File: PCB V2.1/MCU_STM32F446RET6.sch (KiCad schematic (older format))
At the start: 37 parts, among them J1 20021121-00010C4LF, J2 0475890001-MicroUSBPort, SW1 B3U-1000P, U1 STM32F446RET6_-_TQFP64, X1 ABM3B8.000MHZB2T, X2 ABS07-32.768KHZ-9-T

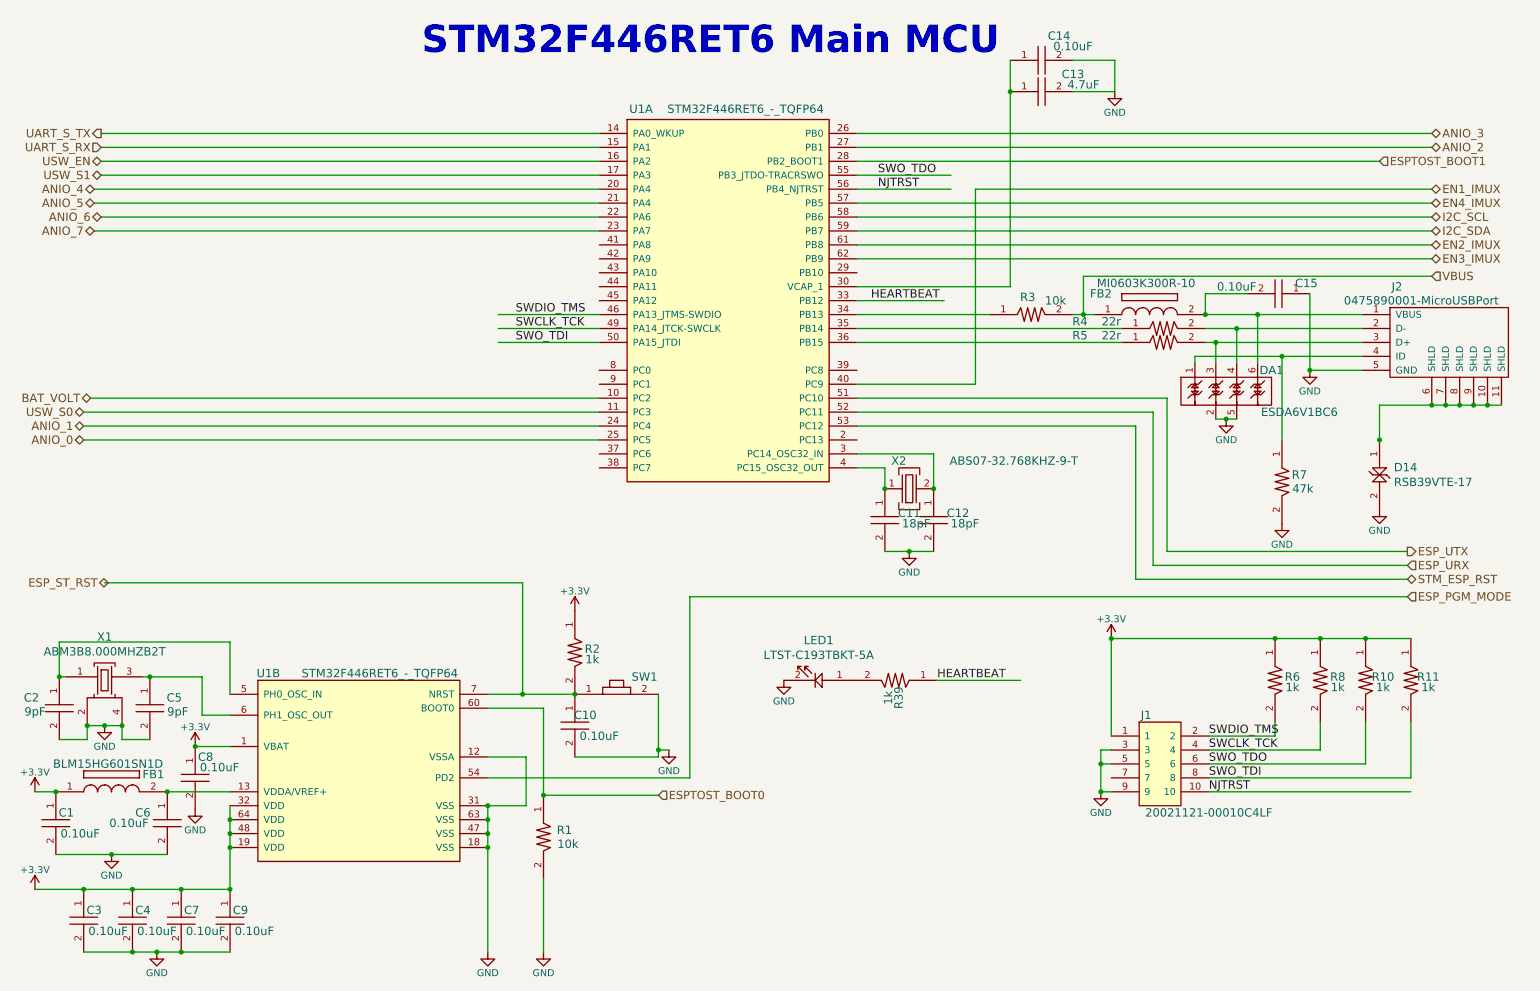
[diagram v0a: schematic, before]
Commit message: App Notes
App notes added to datasheets folder.
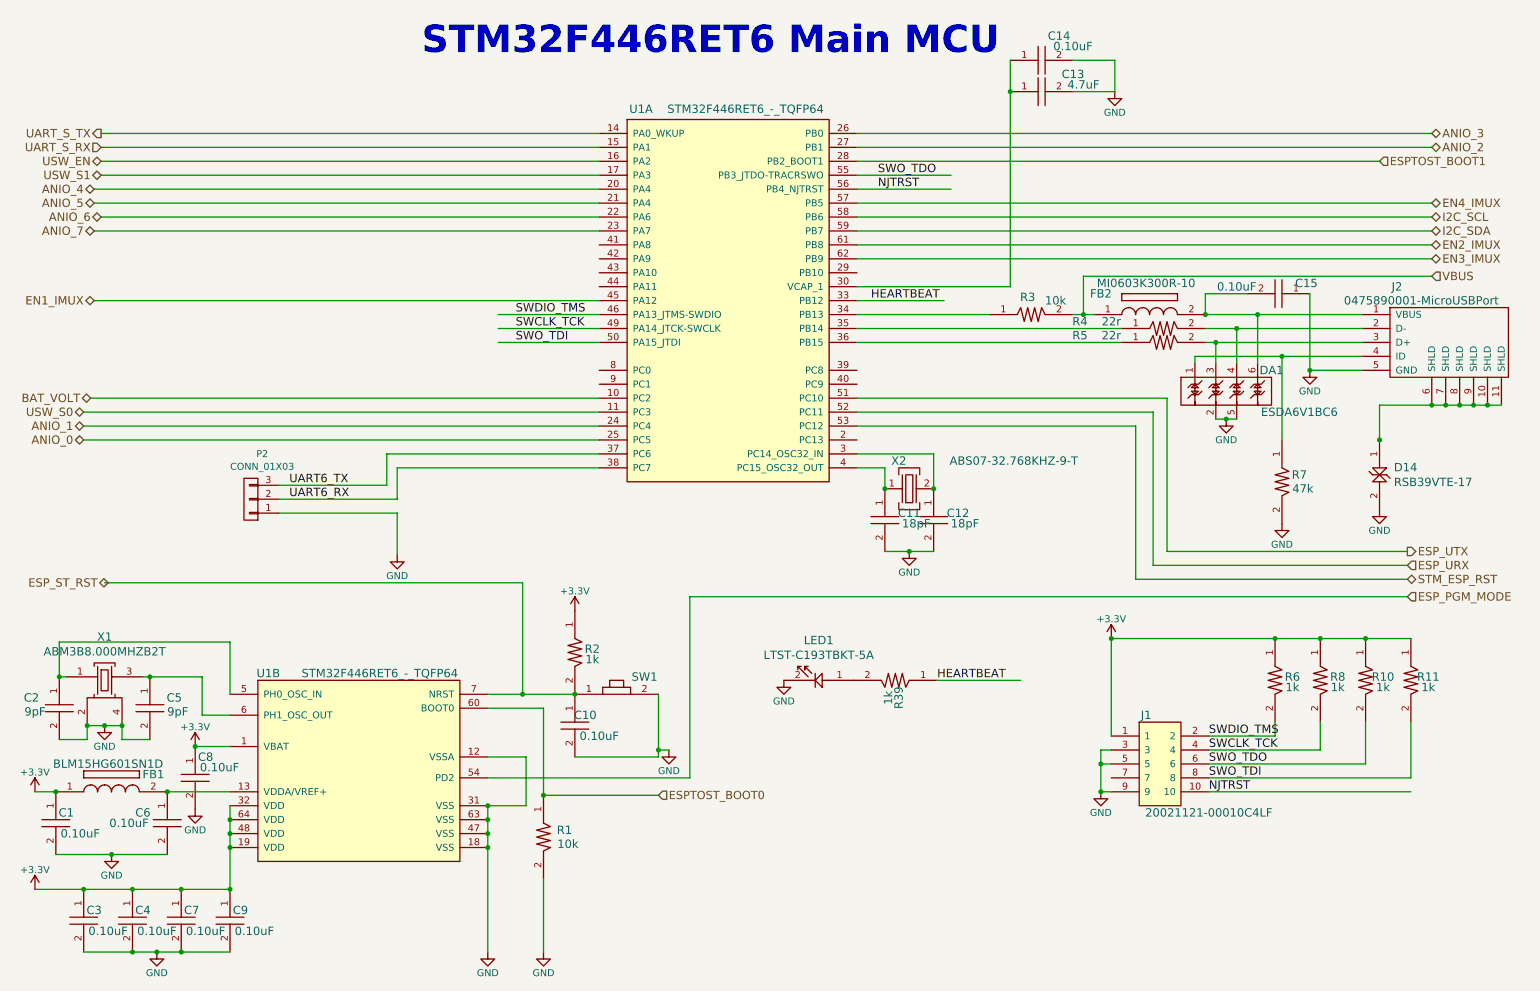
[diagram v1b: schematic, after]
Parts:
- added P2: CONN_01X03, Pin_Headers:Pin_Header_Straight_1x03, symbol CONN_01X03
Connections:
- net labels added: UART6_RX, UART6_TX
- wire segments 122 -> 128
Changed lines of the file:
@@
 Text HLabel 10600 1550 2    60   BiDi ~ 0
 ANIO_2
-Text HLabel 10600 1850 2    60   BiDi ~ 0
+Text HLabel 1000 2650 0    60   BiDi ~ 0
 EN1_IMUX
 Text HLabel 10600 1950 2    60   BiDi ~ 0
@@
 $EndComp
 $Comp
-L GND #PWR4
+L GND #PWR01
 U 1 1 57D43B63
 P 1125 6625
-F 0 "#PWR4" H 1125 6375 50  0001 C CNN
+F 0 "#PWR01" H 1125 6375 50  0001 C CNN
 F 1 "GND" H 1125 6475 50  0000 C CNN
 F 2 "" H 1125 6625 50  0000 C CNN
@@
 $EndComp
 $Comp
-L GND #PWR5
+L GND #PWR02
 U 1 1 57D43E04
 P 1450 7325
-F 0 "#PWR5" H 1450 7075 50  0001 C CNN
+F 0 "#PWR02" H 1450 7075 50  0001 C CNN
 F 1 "GND" H 1450 7175 50  0000 C CNN
 F 2 "" H 1450 7325 50  0000 C CNN
@@
 $EndComp
 $Comp
-L +3.3V #PWR1
+L +3.3V #PWR03
 U 1 1 57D443BB
 P 575 6175
-F 0 "#PWR1" H 575 6025 50  0001 C CNN
+F 0 "#PWR03" H 575 6025 50  0001 C CNN
 F 1 "+3.3V" H 575 6315 50  0000 C CNN
 F 2 "" H 575 6175 50  0000 C CNN
@@
 $EndComp
 $Comp
-L +3.3V #PWR2
+L +3.3V #PWR04
 U 1 1 57D444DD
 P 575 6875
-F 0 "#PWR2" H 575 6725 50  0001 C CNN
+F 0 "#PWR04" H 575 6725 50  0001 C CNN
 F 1 "+3.3V" H 575 7015 50  0000 C CNN
 F 2 "" H 575 6875 50  0000 C CNN
@@
 $EndComp
 $Comp
-L GND #PWR11
+L GND #PWR05
 U 1 1 57D449FF
 P 5125 5875
-F 0 "#PWR11" H 5125 5625 50  0001 C CNN
+F 0 "#PWR05" H 5125 5625 50  0001 C CNN
 F 1 "GND" H 5125 5725 50  0000 C CNN
 F 2 "" H 5125 5875 50  0000 C CNN
@@
 $EndComp
 $Comp
-L +3.3V #PWR10
+L +3.3V #PWR06
 U 1 1 57D45F91
 P 4450 4875
-F 0 "#PWR10" H 4450 4725 50  0001 C CNN
+F 0 "#PWR06" H 4450 4725 50  0001 C CNN
 F 1 "+3.3V" H 4450 5015 50  0000 C CNN
 F 2 "" H 4450 4875 50  0000 C CNN
@@
 $EndComp
 $Comp
-L GND #PWR8
+L GND #PWR07
 U 1 1 57D46AC6
 P 3825 7325
-F 0 "#PWR8" H 3825 7075 50  0001 C CNN
+F 0 "#PWR07" H 3825 7075 50  0001 C CNN
 F 1 "GND" H 3825 7175 50  0000 C CNN
 F 2 "" H 3825 7325 50  0000 C CNN
@@
 $EndComp
 $Comp
-L GND #PWR9
+L GND #PWR08
 U 1 1 57D47BC2
 P 4225 7325
-F 0 "#PWR9" H 4225 7075 50  0001 C CNN
+F 0 "#PWR08" H 4225 7075 50  0001 C CNN
 F 1 "GND" H 4225 7175 50  0000 C CNN
 F 2 "" H 4225 7325 50  0000 C CNN
@@
 $EndComp
 $Comp
-L GND #PWR3
+L GND #PWR09
 U 1 1 57D49635
 P 1075 5700
-F 0 "#PWR3" H 1075 5450 50  0001 C CNN
+F 0 "#PWR09" H 1075 5450 50  0001 C CNN
 F 1 "GND" H 1075 5550 50  0000 C CNN
 F 2 "" H 1075 5700 50  0000 C CNN
@@
 $EndComp
 $Comp
-L GND #PWR13
+L GND #PWR010
 U 1 1 57D4B2EA
 P 6850 4450
-F 0 "#PWR13" H 6850 4200 50  0001 C CNN
+F 0 "#PWR010" H 6850 4200 50  0001 C CNN
 F 1 "GND" H 6850 4300 50  0000 C CNN
 F 2 "" H 6850 4450 50  0000 C CNN
@@
 $EndComp
 $Comp
-L GND #PWR7
+L GND #PWR011
 U 1 1 57D4C07E
 P 1725 6300
-F 0 "#PWR7" H 1725 6050 50  0001 C CNN
+F 0 "#PWR011" H 1725 6050 50  0001 C CNN
 F 1 "GND" H 1725 6150 50  0000 C CNN
 F 2 "" H 1725 6300 50  0000 C CNN
@@
 $EndComp
 $Comp
-L GND #PWR16
+L GND #PWR012
 U 1 1 57D53F54
 P 8325 1150
-F 0 "#PWR16" H 8325 900 50  0001 C CNN
+F 0 "#PWR012" H 8325 900 50  0001 C CNN
 F 1 "GND" H 8325 1000 50  0000 C CNN
 F 2 "" H 8325 1150 50  0000 C CNN
@@
 $EndComp
 $Comp
-L GND #PWR20
+L GND #PWR013
 U 1 1 57D5C6D5
 P 10225 4150
-F 0 "#PWR20" H 10225 3900 50  0001 C CNN
+F 0 "#PWR013" H 10225 3900 50  0001 C CNN
 F 1 "GND" H 10225 4000 50  0000 C CNN
 F 2 "" H 10225 4150 50  0000 C CNN
@@
 $EndComp
 $Comp
-L GND #PWR18
+L GND #PWR014
 U 1 1 57D5C856
 P 9525 4250
-F 0 "#PWR18" H 9525 4000 50  0001 C CNN
+F 0 "#PWR014" H 9525 4000 50  0001 C CNN
 F 1 "GND" H 9525 4100 50  0000 C CNN
 F 2 "" H 9525 4250 50  0000 C CNN
@@
 $EndComp
 $Comp
-L GND #PWR19
+L GND #PWR015
 U 1 1 57D5C8C7
 P 9725 3150
-F 0 "#PWR19" H 9725 2900 50  0001 C CNN
+F 0 "#PWR015" H 9725 2900 50  0001 C CNN
 F 1 "GND" H 9725 3000 50  0000 C CNN
 F 2 "" H 9725 3150 50  0000 C CNN
@@
 $EndComp
 $Comp
-L GND #PWR17
+L GND #PWR016
 U 1 1 57D5FF55
 P 9125 3500
-F 0 "#PWR17" H 9125 3250 50  0001 C CNN
+F 0 "#PWR016" H 9125 3250 50  0001 C CNN
 F 1 "GND" H 9125 3350 50  0000 C CNN
 F 2 "" H 9125 3500 50  0000 C CNN
@@
 $EndComp
 $Comp
-L +3.3V #PWR15
+L +3.3V #PWR017
 U 1 1 57D61D70
 P 8300 5075
-F 0 "#PWR15" H 8300 4925 50  0001 C CNN
+F 0 "#PWR017" H 8300 4925 50  0001 C CNN
 F 1 "+3.3V" H 8300 5215 50  0000 C CNN
 F 2 "" H 8300 5075 50  0000 C CNN
@@
 	9000 6175 10450 6175
 Wire Wire Line
-	10450 5075 8300 5075
+	8300 5075 10450 5075
 Wire Wire Line
 	8300 5075 8300 5775
@@
 Wire Wire Line
 	9725 2600 9725 3150
-Wire Wire Line
-	10600 1850 7325 1850
-Wire Wire Line
-	7325 1850 7325 3250
-Wire Wire Line
-	7325 3250 6475 3250
 Text Notes 3350 900  0    197  ~ 39
 STM32F446RET6 Main MCU
@@
 Connection ~ 9725 3150
 $Comp
-L +3.3V #PWR6
+L +3.3V #PWR018
 U 1 1 57D91770
 P 1725 5850
-F 0 "#PWR6" H 1725 5700 50  0001 C CNN
+F 0 "#PWR018" H 1725 5700 50  0001 C CNN
 F 1 "+3.3V" H 1725 5990 50  0000 C CNN
 F 2 "" H 1725 5850 50  0000 C CNN
@@
 $EndComp
 $Comp
-L GND #PWR14
+L GND #PWR019
 U 1 1 57DDB978
 P 8225 6175
-F 0 "#PWR14" H 8225 5925 50  0001 C CNN
+F 0 "#PWR019" H 8225 5925 50  0001 C CNN
 F 1 "GND" H 8225 6025 50  0000 C CNN
 F 2 "" H 8225 6175 50  0000 C CNN
@@
 	7050 5375 7650 5375
 $Comp
-L GND #PWR12
+L GND #PWR020
 U 1 1 57E11BCD
 P 5950 5375
-F 0 "#PWR12" H 5950 5125 50  0001 C CNN
+F 0 "#PWR020" H 5950 5125 50  0001 C CNN
 F 1 "GND" H 5950 5225 50  0000 C CNN
 F 2 "" H 5950 5375 50  0000 C CNN
@@
 	1    0    0    -1
 $EndComp
+Wire Wire Line
+	4625 3750 3100 3750
+Wire Wire Line
+	3100 3750 3100 3975
+Wire Wire Line
+	3100 3975 2325 3975
+Wire Wire Line
+	2325 4075 3175 4075
+Wire Wire Line
+	3175 4075 3175 3850
+Wire Wire Line
+	3175 3850 4625 3850
+Wire Wire Line
+	2325 4175 3175 4175
+Wire Wire Line
+	3175 4175 3175 4475
+$Comp
+L GND #PWR021
+U 1 1 57E1EF3A
+P 3175 4475
+F 0 "#PWR021" H 3175 4225 50  0001 C CNN
+F 1 "GND" H 3175 4325 50  0000 C CNN
+F 2 "" H 3175 4475 50  0000 C CNN
+F 3 "" H 3175 4475 50  0000 C CNN
+	1    3175 4475
+	1    0    0    -1
+$EndComp
+Text Label 2400 3975 0    60   ~ 0
+UART6_TX
+Text Label 2400 4075 0    60   ~ 0
+UART6_RX
+$Comp
+L CONN_01X03 P2
+U 1 1 57E24091
+P 2125 4075
+F 0 "P2" H 2044 3750 50  0000 C CNN
+F 1 "CONN_01X03" H 2044 3841 50  0000 C CNN
+F 2 "Pin_Headers:Pin_Header_Straight_1x03" H 2125 4075 50  0001 C CNN
+F 3 "" H 2125 4075 50  0000 C CNN
+	1    2125 4075
+	-1   0    0    1
+$EndComp
+Wire Wire Line
+	4625 2650 1000 2650
 $EndSCHEMATC

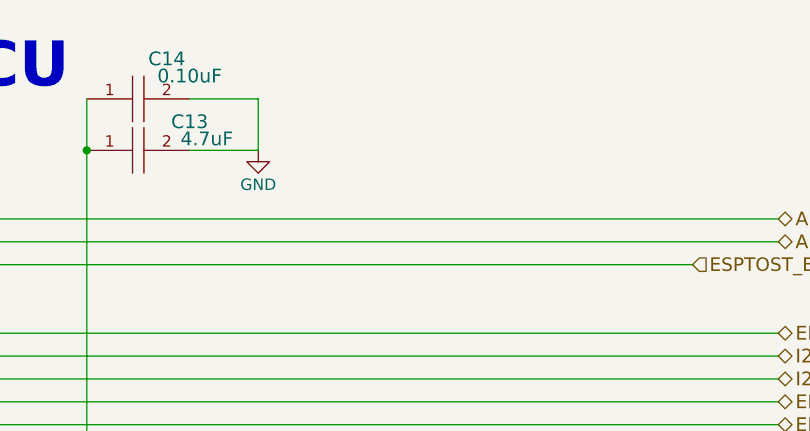
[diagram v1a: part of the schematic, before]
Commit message: DRC Clearing
More DRC errors cleared. Getting board ready for fab.
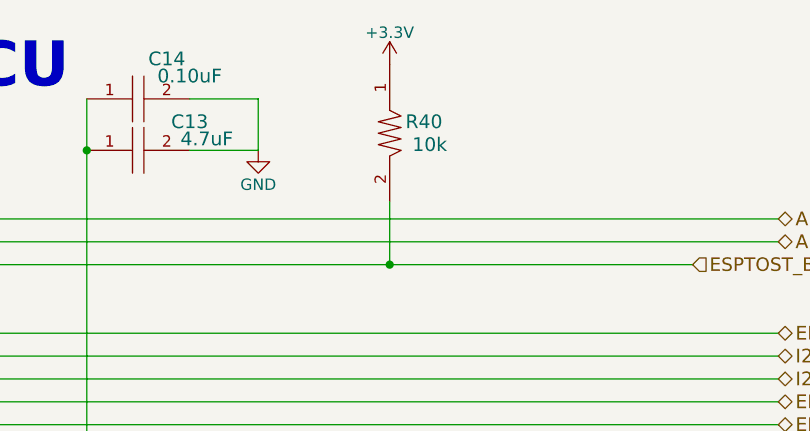
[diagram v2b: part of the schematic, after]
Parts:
- added R40: RC1005F103CS, PCB_Footprints:R0402, symbol RC1005F103CS
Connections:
- wire segments 128 -> 129
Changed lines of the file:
@@
 $EndComp
 $Comp
-L GND #PWR01
+L GND #PWR4
 U 1 1 57D43B63
 P 1125 6625
-F 0 "#PWR01" H 1125 6375 50  0001 C CNN
+F 0 "#PWR4" H 1125 6375 50  0001 C CNN
 F 1 "GND" H 1125 6475 50  0000 C CNN
 F 2 "" H 1125 6625 50  0000 C CNN
@@
 $EndComp
 $Comp
-L GND #PWR02
+L GND #PWR5
 U 1 1 57D43E04
 P 1450 7325
-F 0 "#PWR02" H 1450 7075 50  0001 C CNN
+F 0 "#PWR5" H 1450 7075 50  0001 C CNN
 F 1 "GND" H 1450 7175 50  0000 C CNN
 F 2 "" H 1450 7325 50  0000 C CNN
@@
 $EndComp
 $Comp
-L +3.3V #PWR03
+L +3.3V #PWR1
 U 1 1 57D443BB
 P 575 6175
-F 0 "#PWR03" H 575 6025 50  0001 C CNN
+F 0 "#PWR1" H 575 6025 50  0001 C CNN
 F 1 "+3.3V" H 575 6315 50  0000 C CNN
 F 2 "" H 575 6175 50  0000 C CNN
@@
 $EndComp
 $Comp
-L +3.3V #PWR04
+L +3.3V #PWR2
 U 1 1 57D444DD
 P 575 6875
-F 0 "#PWR04" H 575 6725 50  0001 C CNN
+F 0 "#PWR2" H 575 6725 50  0001 C CNN
 F 1 "+3.3V" H 575 7015 50  0000 C CNN
 F 2 "" H 575 6875 50  0000 C CNN
@@
 $EndComp
 $Comp
-L GND #PWR05
+L GND #PWR12
 U 1 1 57D449FF
 P 5125 5875
-F 0 "#PWR05" H 5125 5625 50  0001 C CNN
+F 0 "#PWR12" H 5125 5625 50  0001 C CNN
 F 1 "GND" H 5125 5725 50  0000 C CNN
 F 2 "" H 5125 5875 50  0000 C CNN
@@
 $EndComp
 $Comp
-L +3.3V #PWR06
+L +3.3V #PWR11
 U 1 1 57D45F91
 P 4450 4875
-F 0 "#PWR06" H 4450 4725 50  0001 C CNN
+F 0 "#PWR11" H 4450 4725 50  0001 C CNN
 F 1 "+3.3V" H 4450 5015 50  0000 C CNN
 F 2 "" H 4450 4875 50  0000 C CNN
@@
 $EndComp
 $Comp
-L GND #PWR07
+L GND #PWR9
 U 1 1 57D46AC6
 P 3825 7325
-F 0 "#PWR07" H 3825 7075 50  0001 C CNN
+F 0 "#PWR9" H 3825 7075 50  0001 C CNN
 F 1 "GND" H 3825 7175 50  0000 C CNN
 F 2 "" H 3825 7325 50  0000 C CNN
@@
 $EndComp
 $Comp
-L GND #PWR08
+L GND #PWR10
 U 1 1 57D47BC2
 P 4225 7325
-F 0 "#PWR08" H 4225 7075 50  0001 C CNN
+F 0 "#PWR10" H 4225 7075 50  0001 C CNN
 F 1 "GND" H 4225 7175 50  0000 C CNN
 F 2 "" H 4225 7325 50  0000 C CNN
@@
 $EndComp
 $Comp
-L GND #PWR09
+L GND #PWR3
 U 1 1 57D49635
 P 1075 5700
-F 0 "#PWR09" H 1075 5450 50  0001 C CNN
+F 0 "#PWR3" H 1075 5450 50  0001 C CNN
 F 1 "GND" H 1075 5550 50  0000 C CNN
 F 2 "" H 1075 5700 50  0000 C CNN
@@
 $EndComp
 $Comp
-L GND #PWR010
+L GND #PWR14
 U 1 1 57D4B2EA
 P 6850 4450
-F 0 "#PWR010" H 6850 4200 50  0001 C CNN
+F 0 "#PWR14" H 6850 4200 50  0001 C CNN
 F 1 "GND" H 6850 4300 50  0000 C CNN
 F 2 "" H 6850 4450 50  0000 C CNN
@@
 $EndComp
 $Comp
-L GND #PWR011
+L GND #PWR7
 U 1 1 57D4C07E
 P 1725 6300
-F 0 "#PWR011" H 1725 6050 50  0001 C CNN
+F 0 "#PWR7" H 1725 6050 50  0001 C CNN
 F 1 "GND" H 1725 6150 50  0000 C CNN
 F 2 "" H 1725 6300 50  0000 C CNN
@@
 $EndComp
 $Comp
-L GND #PWR012
+L GND #PWR17
 U 1 1 57D53F54
 P 8325 1150
-F 0 "#PWR012" H 8325 900 50  0001 C CNN
+F 0 "#PWR17" H 8325 900 50  0001 C CNN
 F 1 "GND" H 8325 1000 50  0000 C CNN
 F 2 "" H 8325 1150 50  0000 C CNN
@@
 $EndComp
 $Comp
-L GND #PWR013
+L GND #PWR22
 U 1 1 57D5C6D5
 P 10225 4150
-F 0 "#PWR013" H 10225 3900 50  0001 C CNN
+F 0 "#PWR22" H 10225 3900 50  0001 C CNN
 F 1 "GND" H 10225 4000 50  0000 C CNN
 F 2 "" H 10225 4150 50  0000 C CNN
@@
 $EndComp
 $Comp
-L GND #PWR014
+L GND #PWR20
 U 1 1 57D5C856
 P 9525 4250
-F 0 "#PWR014" H 9525 4000 50  0001 C CNN
+F 0 "#PWR20" H 9525 4000 50  0001 C CNN
 F 1 "GND" H 9525 4100 50  0000 C CNN
 F 2 "" H 9525 4250 50  0000 C CNN
@@
 $EndComp
 $Comp
-L GND #PWR015
+L GND #PWR21
 U 1 1 57D5C8C7
 P 9725 3150
-F 0 "#PWR015" H 9725 2900 50  0001 C CNN
+F 0 "#PWR21" H 9725 2900 50  0001 C CNN
 F 1 "GND" H 9725 3000 50  0000 C CNN
 F 2 "" H 9725 3150 50  0000 C CNN
@@
 $EndComp
 $Comp
-L GND #PWR016
+L GND #PWR19
 U 1 1 57D5FF55
 P 9125 3500
-F 0 "#PWR016" H 9125 3250 50  0001 C CNN
+F 0 "#PWR19" H 9125 3250 50  0001 C CNN
 F 1 "GND" H 9125 3350 50  0000 C CNN
 F 2 "" H 9125 3500 50  0000 C CNN
@@
 $EndComp
 $Comp
-L +3.3V #PWR017
+L +3.3V #PWR16
 U 1 1 57D61D70
 P 8300 5075
-F 0 "#PWR017" H 8300 4925 50  0001 C CNN
+F 0 "#PWR16" H 8300 4925 50  0001 C CNN
 F 1 "+3.3V" H 8300 5215 50  0000 C CNN
 F 2 "" H 8300 5075 50  0000 C CNN
@@
 Connection ~ 9725 3150
 $Comp
-L +3.3V #PWR018
+L +3.3V #PWR6
 U 1 1 57D91770
 P 1725 5850
-F 0 "#PWR018" H 1725 5700 50  0001 C CNN
+F 0 "#PWR6" H 1725 5700 50  0001 C CNN
 F 1 "+3.3V" H 1725 5990 50  0000 C CNN
 F 2 "" H 1725 5850 50  0000 C CNN
@@
 $EndComp
 $Comp
-L GND #PWR019
+L GND #PWR15
 U 1 1 57DDB978
 P 8225 6175
-F 0 "#PWR019" H 8225 5925 50  0001 C CNN
+F 0 "#PWR15" H 8225 5925 50  0001 C CNN
 F 1 "GND" H 8225 6025 50  0000 C CNN
 F 2 "" H 8225 6175 50  0000 C CNN
@@
 	7050 5375 7650 5375
 $Comp
-L GND #PWR020
+L GND #PWR13
 U 1 1 57E11BCD
 P 5950 5375
-F 0 "#PWR020" H 5950 5125 50  0001 C CNN
+F 0 "#PWR13" H 5950 5125 50  0001 C CNN
 F 1 "GND" H 5950 5225 50  0000 C CNN
 F 2 "" H 5950 5375 50  0000 C CNN
@@
 	3175 4175 3175 4475
 $Comp
-L GND #PWR021
+L GND #PWR8
 U 1 1 57E1EF3A
 P 3175 4475
-F 0 "#PWR021" H 3175 4225 50  0001 C CNN
+F 0 "#PWR8" H 3175 4225 50  0001 C CNN
 F 1 "GND" H 3175 4325 50  0000 C CNN
 F 2 "" H 3175 4475 50  0000 C CNN
@@
 Wire Wire Line
 	4625 2650 1000 2650
+$Comp
+L RC1005F103CS R40
+U 1 1 57E383E7
+P 8900 1075
+F 0 "R40" V 8850 1225 60  0000 C CNN
+F 1 "RC1005F103CS" H 8900 925 60  0001 C CNN
+F 2 "PCB_Footprints:R0402" H 8500 1325 60  0001 C CNN
+F 3 "https://media.digikey.com/pdf/Data%20Sheets/Samsung%20PDFs/RC_Series_ds.pdf" H 8600 1525 60  0001 C CNN
+F 4 "0.00173 @ 5000" H 10450 3025 60  0001 C CNN "Cost"
+F 5 "5 Sept 2016" H 8800 1625 60  0001 C CNN "Date Created"
+F 6 "5 Sept 2016" H 8900 1725 60  0001 C CNN "Date Modified"
+F 7 "Adam Vadala-Roth" H 9000 1825 60  0001 C CNN "Designer"
+F 8 "0.4mm" H 9100 1925 60  0001 C CNN "Height"
+F 9 "Yes" H 9200 2025 60  0001 C CNN "RHoS?"
+F 10 "Samsung Electro-Mechanics America, Inc." H 9300 2125 60  0001 C CNN "MFR"
+F 11 "RC1005F103CS" H 9400 2225 60  0001 C CNN "MFR#"
+F 12 "SMT/SMD" H 9500 2325 60  0001 C CNN "Mounting"
+F 13 "2" H 9600 2425 60  0001 C CNN "Pin Count#"
+F 14 "Active" H 9700 2525 60  0001 C CNN "Status"
+F 15 "1%" H 9800 2625 60  0001 C CNN "Tolerance"
+F 16 "passive" H 9900 2725 60  0001 C CNN "Type"
+F 17 "N/A" H 10000 2825 60  0001 C CNN "Voltage"
+F 18 "1/16" H 10100 2925 60  0001 C CNN "Wattage"
+F 19 "10k" V 8950 1250 60  0000 C CNN "Component-Value"
+F 20 "RES SMD 10K OHM 1% 1/16W 0402" H 10300 3125 60  0001 C CNN "Description"
+	1    8900 1075
+	0    1    1    0
+$EndComp
+$Comp
+L +3.3V #PWR18
+U 1 1 57E391E0
+P 8900 775
+F 0 "#PWR18" H 8900 625 50  0001 C CNN
+F 1 "+3.3V" H 8900 915 50  0000 C CNN
+F 2 "" H 8900 775 50  0000 C CNN
+F 3 "" H 8900 775 50  0000 C CNN
+	1    8900 775
+	1    0    0    -1
+$EndComp
+Wire Wire Line
+	8900 1375 8900 1650
+Connection ~ 8900 1650
 $EndSCHEMATC
